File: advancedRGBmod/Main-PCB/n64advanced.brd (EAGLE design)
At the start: 64.5 x 37.7 mm, 112 parts, among them J6 UPS, U1 10CL010YE144, U2 ADV7125/ADV7123, U4 74LVC3G17, U5 S25FLXXXSO8-DUAL, U6 TLV70012DDC, U7 TLV70025DDC

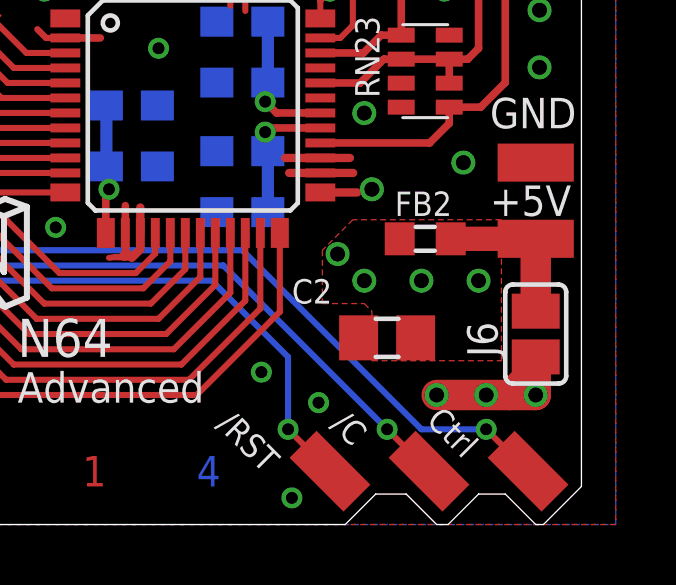
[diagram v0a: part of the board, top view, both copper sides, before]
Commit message: PCB Update: remove jumper for analog power supply I recommend 5V for the analog part anyway. So now the user is forced to use 5V here!
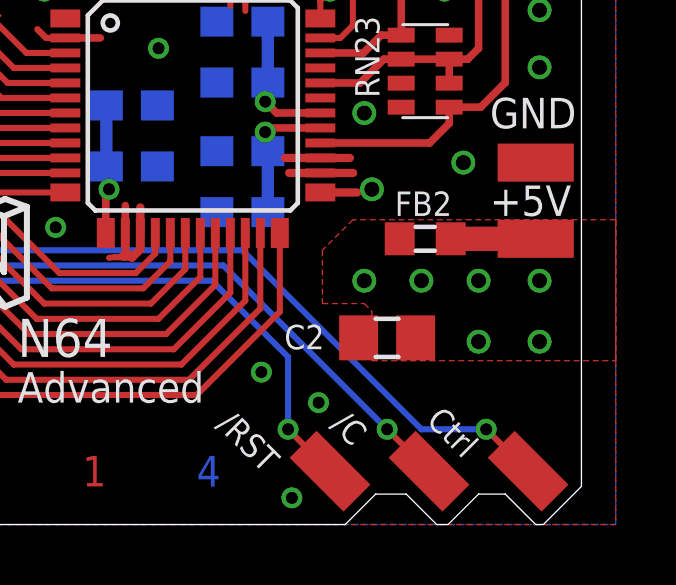
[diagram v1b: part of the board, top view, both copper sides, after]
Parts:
- removed J6: UPS, jumper:SJ
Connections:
- net N$48: no longer J6.2
- net VCCIO: no longer J6.1
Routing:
- net VCCIO: track 84.7 -> 72.2 mm, vias 32 -> 29
- net N$48: track 5.25 -> 2.83 mm
- net +5V: vias 10 -> 12
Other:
- board text added: "N64A_20180205"
- board text added: "PCB Design (c) 2017-2018 Peter Bartmann"
- board text removed: "J6"
- board text removed: "N64A_20171204"
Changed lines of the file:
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@@
 <?xml version="1.0" encoding="utf-8"?>
 <!DOCTYPE eagle SYSTEM "eagle.dtd">
-<eagle version="8.4.3">
+<eagle version="8.6.0">
 <drawing>
 <settings>
@@
 <layer number="48" name="Document" color="7" fill="1" visible="no" active="yes"/>
 <layer number="49" name="Reference" color="7" fill="1" visible="no" active="yes"/>
-<layer number="51" name="tDocu" color="7" fill="1" visible="no" active="yes"/>
+<layer number="51" name="tDocu" color="7" fill="1" visible="yes" active="yes"/>
 <layer number="52" name="bDocu" color="7" fill="1" visible="yes" active="yes"/>
 <layer number="90" name="Modules" color="5" fill="1" visible="no" active="no"/>
@@
 <text x="61.849" y="10.287" size="1.016" layer="25" font="vector" ratio="15">+5V</text>
 <text x="58.674" y="10.287" size="0.8128" layer="25" font="vector" ratio="15">FB2</text>
-<text x="55.245" y="7.366" size="0.8128" layer="25" font="vector" ratio="15">C2</text>
-<text x="62.103" y="5.588" size="1.016" layer="25" font="vector" ratio="15" rot="R90">J6</text>
+<text x="54.991" y="5.842" size="0.8128" layer="25" font="vector" ratio="15">C2</text>
 <text x="52.705" y="3.302" size="0.8128" layer="25" font="vector" ratio="15" rot="R315">/RST</text>
 <text x="56.515" y="3.302" size="0.8128" layer="25" font="vector" ratio="15" rot="R315">/C</text>
@@
 <circle x="32.766" y="0.508" radius="0.05679375" width="0.3048" layer="25"/>
 <circle x="29.464" y="37.211" radius="0.05679375" width="0.3048" layer="25"/>
-<text x="10.668" y="1.27" size="1.016" layer="26" font="vector" ratio="12" rot="MR0" align="center">N64A_20171204</text>
+<text x="10.668" y="1.27" size="1.016" layer="26" font="vector" ratio="12" rot="MR0" align="center">N64A_20180205</text>
 <wire x1="11.303" y1="30.861" x2="11.303" y2="33.909" width="0.1524" layer="25"/>
 <wire x1="11.303" y1="33.909" x2="12.573" y2="35.179" width="0.1524" layer="25"/>
@@
 <vertex x="15.8242" y="11.43"/>
 </polygon>
+<text x="0" y="-2.032" size="1.016" layer="51" font="vector">PCB Design (c) 2017-2018 Peter Bartmann</text>
 </plain>
 <attributes>
@@
 <param name="checkRestrict" value="0"/>
 <param name="checkStop" value="0"/>
+<param name="checkValues" value="0"/>
 <param name="useDiameter" value="13"/>
 <param name="maxErrors" value="50"/>
@@
 <element name="J2" library="jumper" package="SJ_2" value="" x="34.29" y="1.905" smashed="yes">
 <attribute name="VALUE" x="34.1899" y="1.905" size="0.02" layer="27"/>
-</element>
-<element name="J6" library="jumper" package="SJ" value="UPS" x="63.373" y="6.35" smashed="yes" rot="R90">
-<attribute name="VALUE" x="63.373" y="6.7501" size="0.02" layer="27" rot="R90"/>
 </element>
 <element name="P_GND0" library="wirepad@1" package="SMD1,27-2,54" value="" x="1.905" y="29.845" smashed="yes" rot="R90">
@@
 </signal>
 <signal name="VCCIO">
-<contactref element="J6" pad="1"/>
 <contactref element="C111" pad="1"/>
 <contactref element="C102" pad="1"/>
@@
 <wire x1="41.368046875" y1="13.46525" x2="42.260296875" y2="12.573" width="0.254" layer="1"/>
 <wire x1="42.260296875" y1="12.573" x2="42.672" y2="12.573" width="0.254" layer="1"/>
-<via x="63.373" y="4.318" extent="1-16" drill="0.5"/>
-<via x="60.071" y="4.318" extent="1-16" drill="0.5"/>
 <via x="36.449" y="25.654" extent="1-16" drill="0.4"/>
 <via x="40.64" y="21.336" extent="1-16" drill="0.4"/>
@@
 <wire x1="40.64" y1="29.972" x2="39.79" y2="29.972" width="0.2032" layer="1"/>
 <wire x1="39.79" y1="29.972" x2="39.497" y2="30.06" width="0.2032" layer="1"/>
-<wire x1="62.493428125" y1="4.318" x2="63.373" y2="4.318" width="1.016" layer="1"/>
-<wire x1="62.493428125" y1="4.318" x2="60.071" y2="4.318" width="1.016" layer="1"/>
-<wire x1="63.373" y1="5.588" x2="63.373" y2="4.318" width="1.016" layer="1"/>
-<wire x1="60.071" y1="4.318" x2="62.103" y2="4.318" width="0.4064" layer="1"/>
-<wire x1="62.103" y1="4.318" x2="63.373" y2="5.588" width="0.4064" layer="1"/>
-<via x="61.722" y="4.318" extent="1-16" drill="0.5"/>
-<wire x1="61.722" y1="4.318" x2="62.493428125" y2="4.318" width="0.4064" layer="1"/>
-<wire x1="60.071" y1="4.318" x2="63.373" y2="4.318" width="1.016" layer="15"/>
 <contactref element="FB4" pad="1"/>
 <via x="10.668" y="36.957" extent="1-16" drill="0.5"/>
@@
 <contactref element="P_VCC_5V" pad="1"/>
 <contactref element="FB2" pad="1"/>
-<contactref element="J6" pad="2"/>
-<wire x1="63.373" y1="7.112" x2="63.373" y2="9.525" width="1.016" layer="1"/>
 <wire x1="63.373" y1="9.525" x2="60.54" y2="9.525" width="0.8128" layer="1"/>
 </signal>
@@
 <contactref element="C2" pad="1"/>
 <via x="61.468" y="8.128" extent="1-16" drill="0.5"/>
-<via x="56.769" y="9.017" extent="1-16" drill="0.5"/>
 <via x="57.658" y="8.128" extent="1-16" drill="0.5"/>
 <via x="49.149" y="11.176" extent="1-16" drill="0.4"/>
@@
 <wire x1="46.568" y1="35.9" x2="46.609" y2="35.941" width="0.254" layer="1"/>
 <polygon width="0.3048" layer="1">
-<vertex x="62.23" y="10.16"/>
+<vertex x="66.04" y="10.16"/>
 <vertex x="57.277" y="10.16"/>
 <vertex x="56.261" y="9.144"/>
@@
 <vertex x="57.912" y="7.112"/>
 <vertex x="57.912" y="5.461"/>
-<vertex x="62.23" y="5.461"/>
+<vertex x="66.04" y="5.461"/>
 </polygon>
 <via x="59.563" y="8.128" extent="1-16" drill="0.5"/>
@@
 <vertex x="66.04" y="38.1"/>
 </polygon>
+<via x="61.468" y="6.096" extent="1-16" drill="0.5"/>
+<via x="63.5" y="8.128" extent="1-16" drill="0.5"/>
+<via x="63.5" y="6.096" extent="1-16" drill="0.5"/>
 </signal>
 <signal name="CSYNC#">

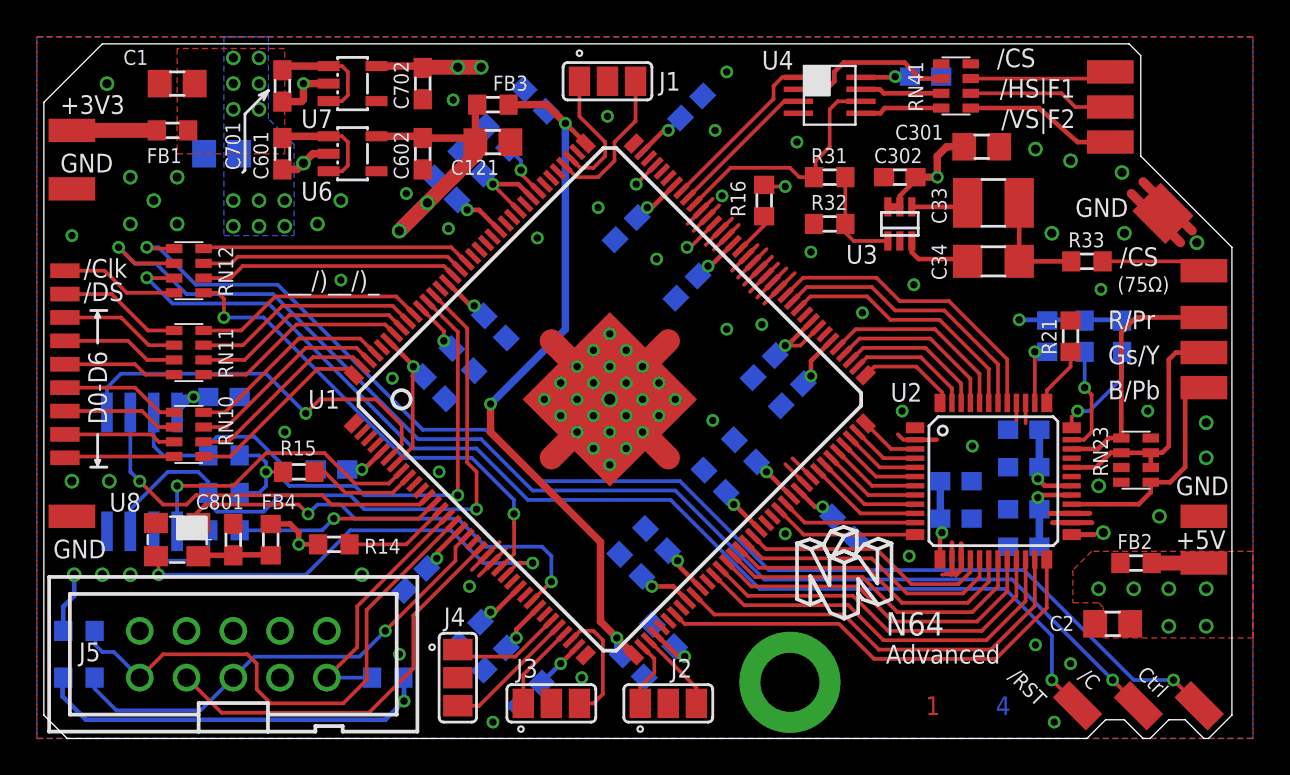
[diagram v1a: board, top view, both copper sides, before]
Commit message: update PCB - add fields for GND shield fingers and remove pad for /COLD
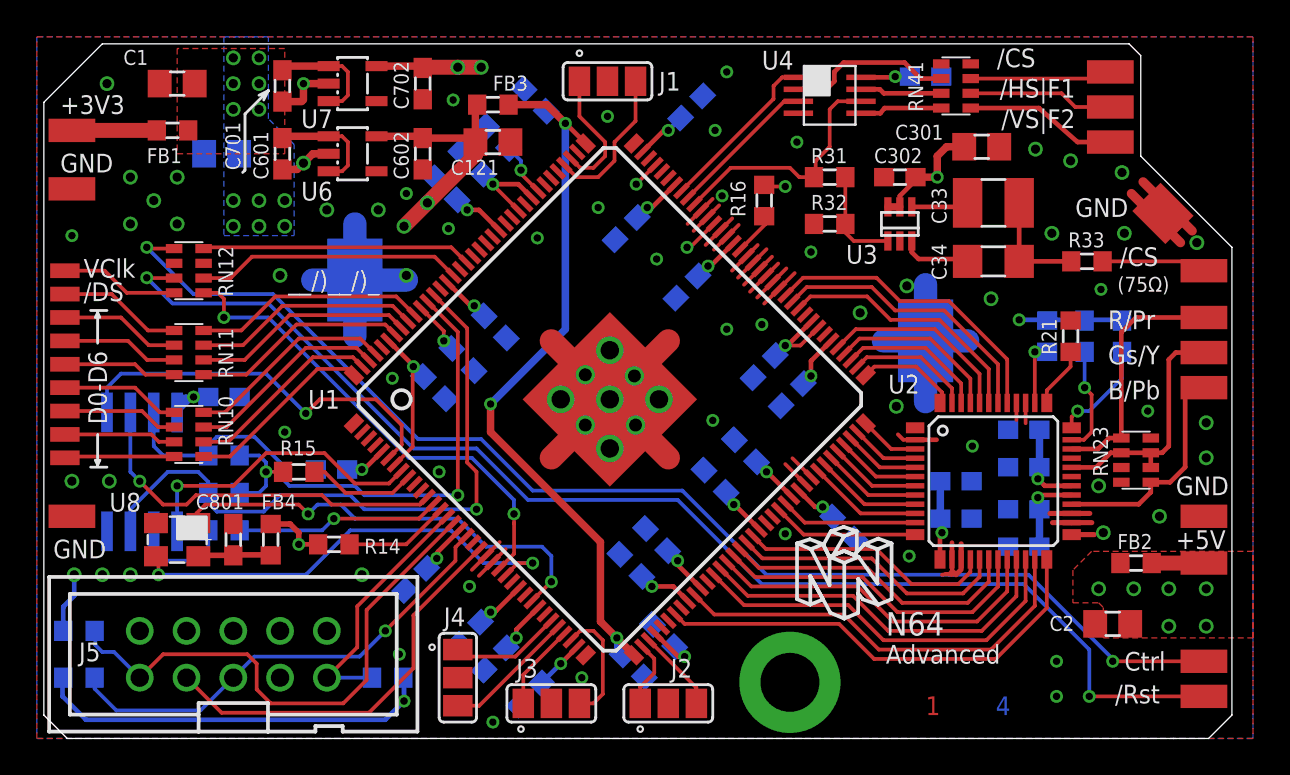
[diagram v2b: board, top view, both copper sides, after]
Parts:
- removed /COLD: (no value), wirepad@1:SMD1,27-2,54
- added P_GND_SF1, P_GND_SF2: (no value), snes_div:GND_FINGER_PAD
- moved /RST 6.88 mm to (63.4, 2.29), turned to 90 degrees
- moved CTRL 2.43 mm to (63.4, 4.19), turned to 90 degrees
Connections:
- removed net N$56: RN12.7, U1.128
- removed net N$67: /COLD.1, RN12.2
- net GND: now also P_GND_SF1.P$1, P_GND_SF2.P$1
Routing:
- net N$67: track 69.1 -> 0.00 mm, vias 2 -> 0
- net GND: track 78.9 -> 101.0 mm, vias 86 -> 73
- net N$56: track 14.4 -> 0.00 mm
- net N$70: track 63.1 -> 69.8 mm
- net VCCINT: track 118.7 -> 118.1 mm
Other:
- outline, holes or cut-outs redrawn
- board text added: "/Rst"
- board text added: "GND Finger"
- board text added: "N64A_20180725"
- board text added: "VClk"
- board text removed: "/C"
- board text removed: "/Clk"
- board text removed: "/RST"
- board text removed: "N64A_20180205"
